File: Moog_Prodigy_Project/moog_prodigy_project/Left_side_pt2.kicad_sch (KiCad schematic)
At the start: 74 parts, among them J7 Conn_01x02_Socket, Q4 BC107, Q7 BC549, SW3 Switch_4x4, SW4 SW_Slide_DPDT_3x3, SW5 Switch_4x4, U2B2 OPA134, U4B1 OPA134, U6 NE5532, U7 NE5532, U8 LT1011CN8

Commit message: MOOG prodigy final 03.07.2026
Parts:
- R46: value 4K75 -> 4K75 1%
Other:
- note added: "NAPOMENA 1 Kondenzatori: C49,C50,C51,C52,C53, C54,C55,C56,C57,C58 su vrednosti 100n i oni su kvalitetniji"
- note added: "NAPOMENA 2 Otpornici cija je vrednost: 63K4, 18K2, 4K75, 6K81, 51M, 2.4M su otpornici iz E96 serije (1%) Ostali orpotnici su iz serije E24 (5%)"
- note removed: "NAPOMENA Kondenzatori: C49,C50,C51,C52,C53, C54,C55,C56,C57,C58 su vrednosti 100n i oni su kvalitetniji"
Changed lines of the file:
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@@
 		)
 	)
-	(text "NAPOMENA\nKondenzatori:\nC49,C50,C51,C52,C53,\nC54,C55,C56,C57,C58\nsu vrednosti 100n i oni su kvalitetniji"
+	(text "NAPOMENA 1\nKondenzatori:\nC49,C50,C51,C52,C53,\nC54,C55,C56,C57,C58\nsu vrednosti 100n i oni su kvalitetniji"
 		(exclude_from_sim no)
 		(at 196.596 159.258 0)
@@
 		)
 	)
+	(text "NAPOMENA 2\nOtpornici cija je vrednost:\n63K4, 18K2, 4K75, 6K81, 51M, 2.4M\nsu otpornici iz E96 serije (1%)\nOstali orpotnici su iz serije E24 (5%)"
+		(exclude_from_sim no)
+		(at 235.712 159.258 0)
+		(effects
+			(font
+				(size 1.27 1.27)
+				(thickness 0.254)
+				(bold yes)
+			)
+			(justify left)
+		)
+	)
 	(text "5_UIE"
 		(exclude_from_sim no)
@@
 			)
 		)
-		(property "Value" "4K75"
+		(property "Value" "4K75 1%"
 			(at 95.25 65.024 90)
 			(effects

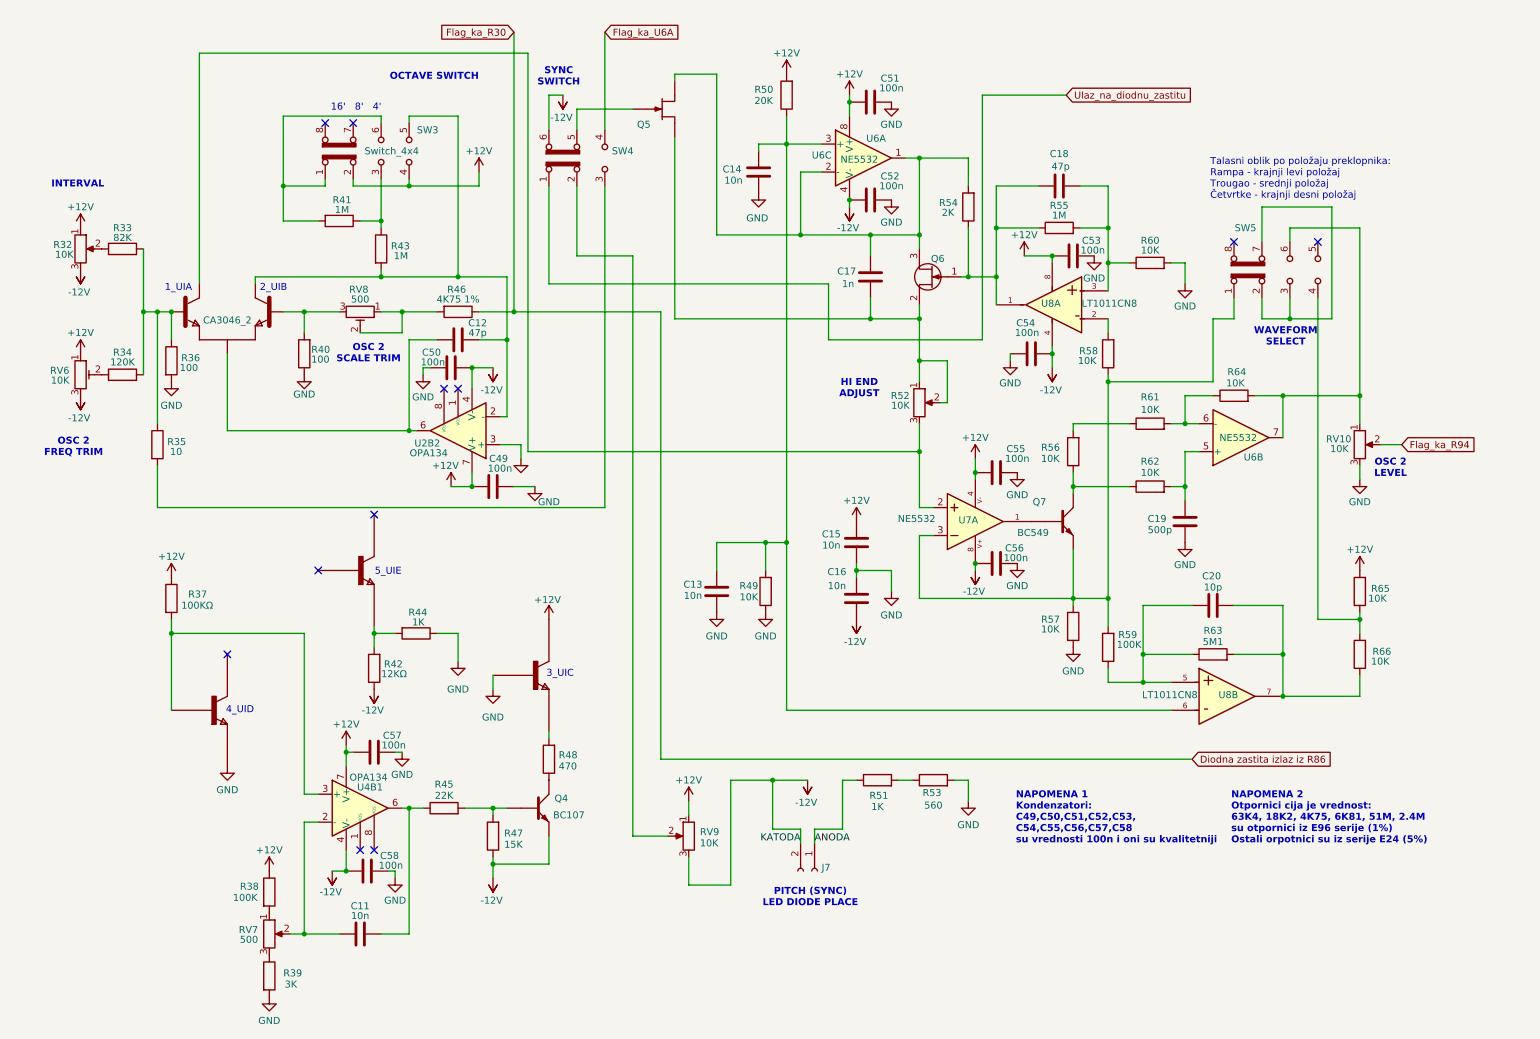
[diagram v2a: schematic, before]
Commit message: Moog prodigy fix 3
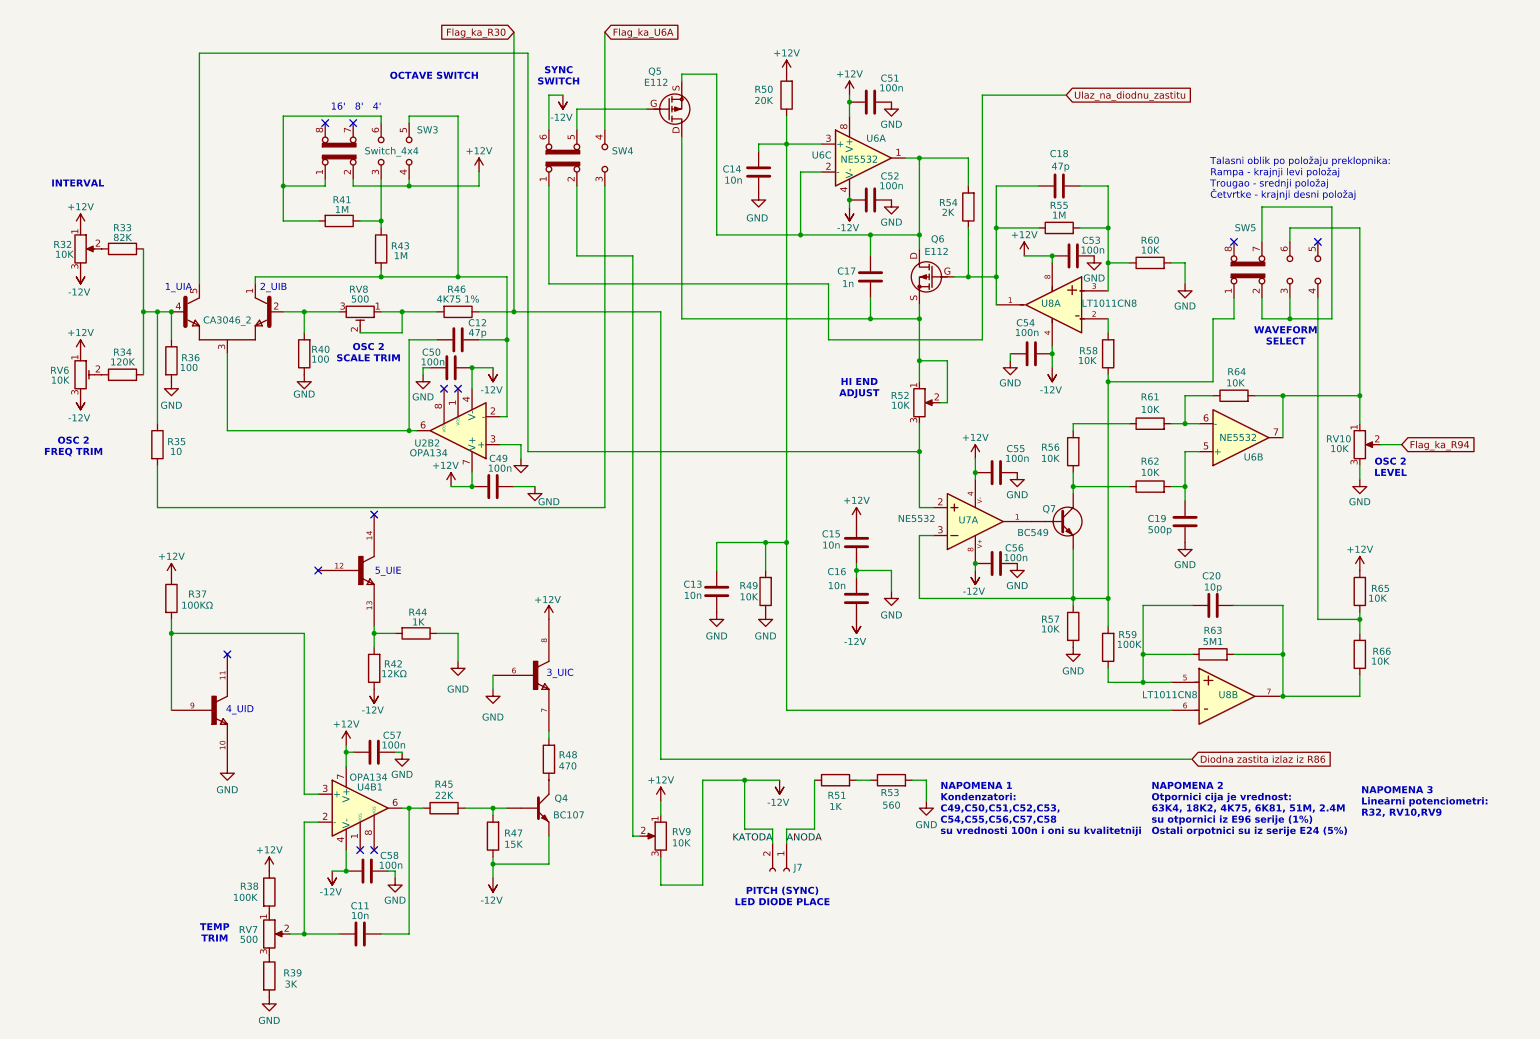
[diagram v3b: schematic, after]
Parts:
- Q5, Q6: value ~ -> E112
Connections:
- net +12V: now also CA3046_2.8; no longer CA3046_2.
- net GND: now also CA3046_2.10, CA3046_2.6; no longer CA3046_2.
- net at R37.2, U4B1.3 (+): now also CA3046_2.9; no longer CA3046_2.
- net at R33.2, R34.2, R35.1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: now also CA3046_2.4; no longer CA3046_2.
- net at C18.1, R54.1, R55.1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: now also Q6.G; no longer Q6.1
- net at R40.2, RV8.3: now also CA3046_2.2; no longer CA3046_2.
- net at C17.1, R52.1, R52.2: now also Q5.D, Q6.S; no longer Q5., Q6.2
- net at C17.2, R54.2, U6.1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: now also Q5.S, Q6.D; no longer Q5., Q6.3
- net at SW4.5 (B): now also Q5.G; no longer Q5.
- net at R42.2, R44.2: now also CA3046_2.13; no longer CA3046_2.
- net at C12.2, R43.2, SW3.5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: now also CA3046_2.1; no longer CA3046_2.
- net at R52.3, U7.2: now also CA3046_2.5; no longer CA3046_2.
- net at R48.2: now also CA3046_2.7; no longer CA3046_2.
- net at C12.1, U2B2.6: now also CA3046_2.3; no longer CA3046_2.
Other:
- note added: "NAPOMENA 3 Linearni potenciometri: R32, RV10,RV9"
- note added: "TEMP TRIM"
- moved on the sheet: J7, R51, R53, RV9

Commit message: treba mi da preraspodelim CA 3046
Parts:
- R37: value 100KΩ -> 100K
- renumbered CA3046_2 to CA3046
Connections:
- net +12V: no longer U8.8
- net at C13.2, C14.2, R49.2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: no longer U8.6
- net at C20.1, R63.2, R66.1: no longer U8.7
- net at C20.2, R59.1, R63.1: no longer U8.5
- no-connect marks 11 -> 7
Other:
- moved on the sheet: C18, C51, R55, U8B

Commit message: 04.07.2026 Dodati tolerancije, E94, prosiriti spisak
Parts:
- Q4: value BC107 -> BC549
- renumbered R32 to R32_LIN, RV10 to RV10_LIN, RV9 to RV9_LIN
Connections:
- net +12V: now also U8.8
- net at C18.2, R55.2, R60.1: now also U8. (-); no longer U8.3 (+)
- net at R58.2: now also U8. (-); no longer U8.2 (-)
- net at C13.2, C14.2, R49.2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: now also U8. (-)
- net at C20.1, R63.2, R66.1: now also U8.7
- net at C20.2, R59.1, R63.1: now also U8. (-)
- net ANODA renamed ANODE
- net Flag_ka_R94 renamed Flag_to_R94
- net Ulaz_na_diodnu_zastitu renamed Input_to_diode_protection
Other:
- note added: "Signal waveform depending on switch position: Ramp - left position Triangle - center position Square - right position"
- note removed: "NAPOMENA 3 Linearni potenciometri: R32, RV10,RV9"
- note removed: "Talasni oblik po položaju preklopnika: Rampa - krajnji levi položaj Trougao - srednji položaj Četvrtke - krajnji desni položaj"
- moved on the sheet: R40, R57, R63, RV10_LIN

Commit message: 07.06.2026 fix 3
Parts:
- added R118: 11, Resistor_THT:R_Axial_DIN0207_L6.3mm_D2.5mm_P7.62mm_Horizontal, symbol Device:R
- added R119: 2K, Resistor_THT:R_Axial_DIN0207_L6.3mm_D2.5mm_P7.62mm_Horizontal, symbol Device:R
- added R120: 200, Resistor_THT:R_Axial_DIN0207_L6.3mm_D2.5mm_P7.62mm_Horizontal, symbol Device:R
- R33: value 82K -> 82K5
- R39: value 3K -> 3K01
- R42: value 12KΩ -> 11K8
- R45: value 22K -> 20K
- R46: value 4K75 1% -> 4K75
- R53: value 560 -> 549
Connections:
- net -12V: now also R120.1; no longer R42.1
- net ANODE: no longer J7.1 (ANODA), R51.1
- net GND: now also R118.2; no longer R53.2
- new net: R118.1, R53.2
- new net: R119.1, R45.2
- new net: R120.2, R42.1
- new net: Q4. (E), R119.2, R47.2
- new net: J7.1 (ANODA), R51.1
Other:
- note removed: "NAPOMENA 2 Otpornici cija je vrednost: 63K4, 18K2, 4K75, 6K81, 51M, 2.4M su otpornici iz E96 serije (1%) Ostali orpotnici su iz serije E24 (5%)"
- moved on the sheet: R42, R51, R53, R63

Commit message: 08.07.2026 fix
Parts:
- removed J7: Conn_01x02_Socket, Connector_PinSocket_2.54mm:PinSocket_1x02_P2.54mm_Vertical, symbol Connector:Conn_01x02_Socket
- removed R118: 11, Resistor_THT:R_Axial_DIN0207_L6.3mm_D2.5mm_P7.62mm_Horizontal, symbol Device:R
- removed R119: 2K, Resistor_THT:R_Axial_DIN0207_L6.3mm_D2.5mm_P7.62mm_Horizontal, symbol Device:R
- removed R53: 549, Resistor_THT:R_Axial_DIN0207_L6.3mm_D2.5mm_P7.62mm_Horizontal, symbol Device:R
- added D7: LED, symbol Device:LED
- R32: renamed from R32_LIN; value 10K -> 10K LIN
- R45: value 20K -> 22K 10%
- R50: value 20K -> 20K 5%
- R51: value 1K -> 1K6 5%
- RV10: renamed from RV10_LIN; value 10K -> 10K LIN
- RV7: symbol Device:R_Potentiometer -> Device:R_Potentiometer_Trim
- RV9: renamed from RV9_LIN; value 10K -> 10K LIN
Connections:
- net -12V: now also D7.1 (K)
- net GND: now also R51.2
- net at R45.2: now also Q4. (E), R47.2
- net at R51.1: now also D7.2 (A)
- net Diodna zastita izlaz iz R86 renamed Flag to R87
- net Flag_to_R94 renamed Flag to R94
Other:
- note added: "LED DIODE"
- note added: "PITCH SYNC CONTROL"
- note added: "PP"
- note removed: "NAPOMENA 1 Kondenzatori: C49,C50,C51,C52,C53, C54,C55,C56,C57,C58 su vrednosti 100n i oni su kvalitetniji"
- note removed: "PITCH (SYNC) LED DIODE PLACE"
- moved on the sheet: R45, R51
